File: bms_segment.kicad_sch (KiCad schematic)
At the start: 95 parts, among them J1 CELL_TAPS, J2 I2C, J5 SWD, J6 I2C, SW1 SW_Push, U1 LMR516xx, U2 STM32F103C8Tx, U3 ADuM1252, U4 MAX14920, U5 MAX11163, U6 REF61xx, Y1 8M

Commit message: bom: Cleanup some BOM fields
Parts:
- C34: Dist (none) -> LCSC; Dist # (none) -> C126576; Mfr (none) -> Murata; Mfr # (none) -> GCM1885C2A101JA16D
- J1: value CELL_TAPS -> Conn_01x13
- J2, J6: value I2C -> Conn_01x04
- J5: value SWD -> Conn_01x05
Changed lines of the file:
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@@
 			)
 		)
-		(property "Value" "CELL_TAPS"
+		(property "Value" "Conn_01x13"
 			(at 58.42 113.03 0)
 			(effects
@@
 			)
 		)
-		(property "Value" "I2C"
+		(property "Value" "Conn_01x04"
 			(at 135.89 67.31 0)
 			(effects
@@
 			)
 		)
-		(property "Value" "SWD"
+		(property "Value" "Conn_01x05"
 			(at 270.51 86.3599 0)
 			(effects
@@
 			)
 		)
-		(property "Value" "I2C"
+		(property "Value" "Conn_01x04"
 			(at 153.67 62.23 0)
 			(effects
@@
 			)
 		)
-		(property "Dist #" ""
+		(property "Dist #" "C126576"
 			(at 162.56 156.21 0)
 			(effects
@@
 			)
 		)
-		(property "Mfr" ""
+		(property "Mfr" "Murata"
 			(at 162.56 156.21 0)
 			(effects
@@
 			)
 		)
-		(property "Mfr #" ""
+		(property "Mfr #" "GCM1885C2A101JA16D"
 			(at 162.56 156.21 0)
 			(effects
@@
 			)
 		)
-		(property "Dist" ""
+		(property "Dist" "LCSC"
 			(at 162.56 156.21 0)
 			(effects

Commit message: *: Create a 3V3 plane and switch to new reset button
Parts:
- SW1: footprint Button_Switch_SMD:SW_Push_SPST_NO_Alps_SKRK -> Button_Switch_SMD:SW_Push_1P1T_NO_Vertical_Wuerth_434133025816; Dist # C720477 -> C139797; Mfr XUNPU -> ALPSALPINE; Mfr # TS-1088-AR02016 -> SKRPACE010
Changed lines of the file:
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@@
 			)
 		)
-		(property "Footprint" "Button_Switch_SMD:SW_Push_SPST_NO_Alps_SKRK"
+		(property "Footprint" "Button_Switch_SMD:SW_Push_1P1T_NO_Vertical_Wuerth_434133025816"
 			(at 270.51 95.25 0)
 			(effects
@@
 			)
 		)
-		(property "Dist #" "C720477"
+		(property "Dist #" "C139797"
 			(at 270.51 100.33 0)
 			(effects
@@
 			)
 		)
-		(property "Mfr" "XUNPU"
+		(property "Mfr" "ALPSALPINE"
 			(at 270.51 100.33 0)
 			(effects
@@
 			)
 		)
-		(property "Mfr #" "TS-1088-AR02016"
+		(property "Mfr #" "SKRPACE010"
 			(at 270.51 100.33 0)
 			(effects

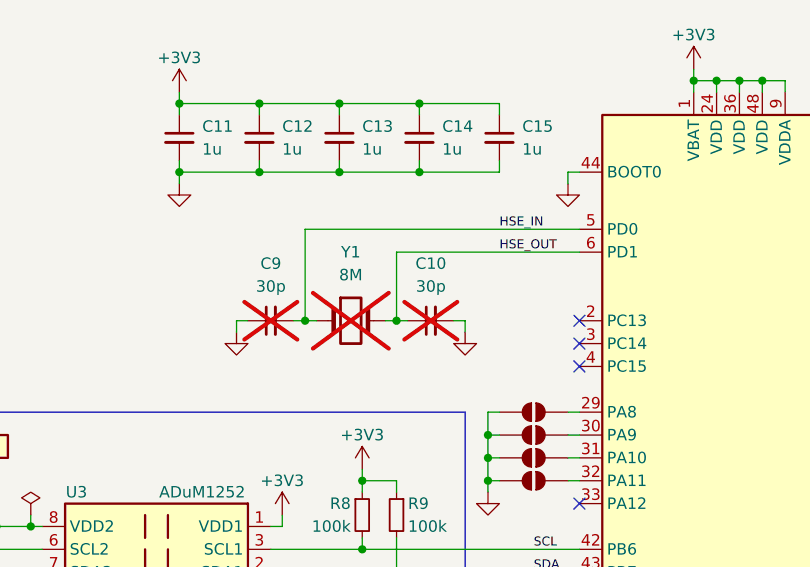
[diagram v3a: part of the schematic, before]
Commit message: schematic: Remove STM crystal
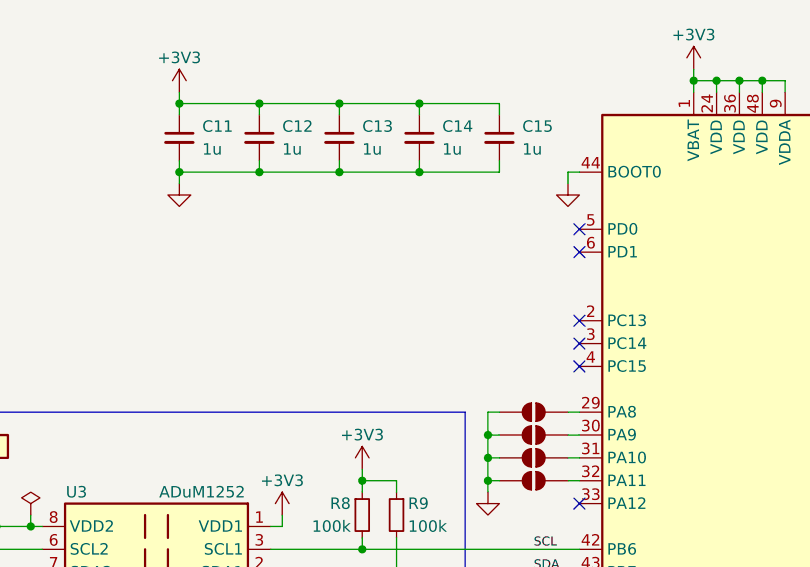
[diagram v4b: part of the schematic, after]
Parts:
- removed C10, C9: 30p, Capacitor_SMD:C_0603_1608Metric, symbol Device:C_Small
- removed Y1: 8M, Crystal:Crystal_SMD_5032-2Pin_5.0x3.2mm, symbol Device:Crystal
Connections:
- net HSE_IN: no longer names the net of U2.5 (PD0)
- net HSE_OUT: no longer names the net of U2.6 (PD1)
- no-connect marks 10 -> 12

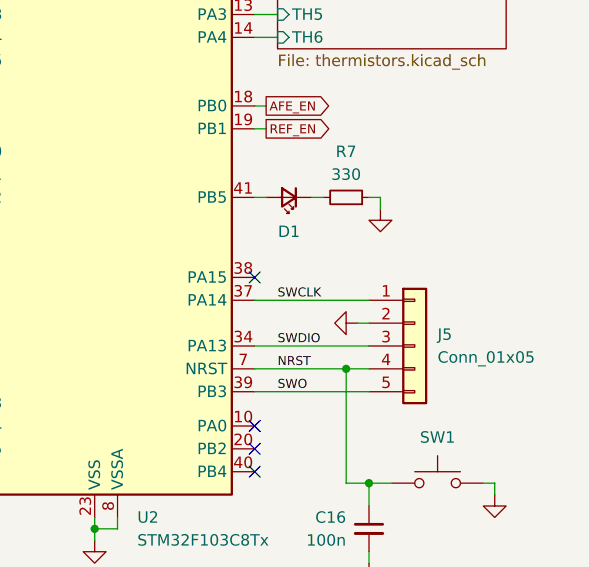
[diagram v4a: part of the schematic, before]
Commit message: schematic: Switch to new SWD header
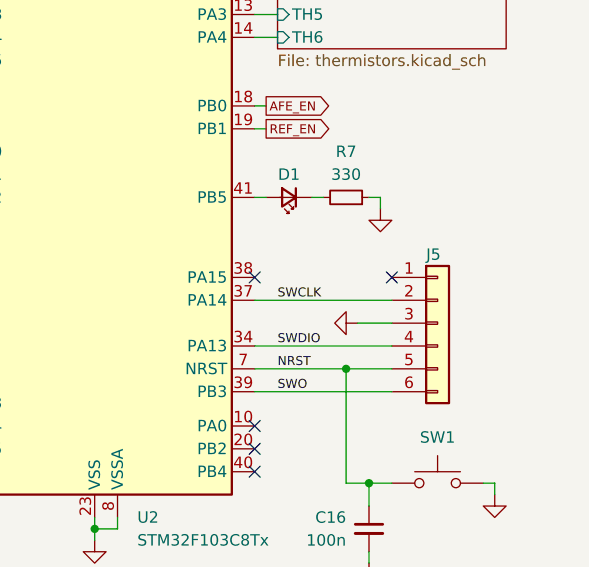
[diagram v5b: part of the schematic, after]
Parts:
- removed J5: Conn_01x05, Connector_PinHeader_2.54mm:PinHeader_1x05_P2.54mm_Vertical, symbol Connector_Generic:Conn_01x05
- added J5: Conn_01x06, yfs:IDC-Connector-2x3, symbol Connector_Generic:Conn_01x06
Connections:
- net GND: now also J5.3 (Pin_3)
- net NRST: now also J5.5 (Pin_5)
- net SWCLK: now also J5.2 (Pin_2)
- net SWDIO: now also J5.4 (Pin_4)
- net SWO: now also J5.6 (Pin_6)
- no-connect marks 12 -> 13
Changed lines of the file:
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@@
 	)
 	(no_connect
+		(at 265.43 77.47)
+	)
+	(no_connect
 		(at 214.63 53.34)
 	)
@@
 	(wire
 		(pts
-			(xy 250.19 85.09) (xy 262.89 85.09)
+			(xy 250.19 85.09) (xy 265.43 85.09)
 		)
 		(stroke
@@
 	(wire
 		(pts
-			(xy 250.19 80.01) (xy 262.89 80.01)
+			(xy 250.19 80.01) (xy 265.43 80.01)
 		)
 		(stroke
@@
 	(wire
 		(pts
-			(xy 250.19 90.17) (xy 262.89 90.17)
+			(xy 250.19 90.17) (xy 265.43 90.17)
 		)
 		(stroke
@@
 	(wire
 		(pts
-			(xy 261.62 82.55) (xy 262.89 82.55)
+			(xy 261.62 82.55) (xy 265.43 82.55)
 		)
 		(stroke
@@
 	(wire
 		(pts
-			(xy 260.35 87.63) (xy 262.89 87.63)
+			(xy 260.35 87.63) (xy 265.43 87.63)
 		)
 		(stroke
@@
 	)
 	(symbol
-		(lib_id "Connector_Generic:Conn_01x05")
-		(at 267.97 85.09 0)
-		(unit 1)
-		(exclude_from_sim no)
-		(in_bom yes)
-		(on_board yes)
-		(dnp no)
-		(fields_autoplaced yes)
-		(property "Reference" "J5"
-			(at 270.51 83.8199 0)
-			(effects
-				(font
-					(size 1.27 1.27)
-				)
-				(justify left)
-			)
-		)
-		(property "Value" "Conn_01x05"
-			(at 270.51 86.3599 0)
-			(effects
-				(font
-					(size 1.27 1.27)
-				)
-				(justify left)
-			)
-		)
-		(property "Footprint" "Connector_PinHeader_2.54mm:PinHeader_1x05_P2.54mm_Vertical"
-			(at 267.97 85.09 0)
-			(effects
-				(font
-					(size 1.27 1.27)
-				)
-				(hide yes)
-			)
-		)
-		(property "Datasheet" "~"
-			(at 267.97 85.09 0)
-			(effects
-				(font
-					(size 1.27 1.27)
-				)
-				(hide yes)
-			)
-		)
-		(property "Description" "Generic connector, single row, 01x05, script generated (kicad-library-utils/schlib/autogen/connector/)"
-			(at 267.97 85.09 0)
-			(effects
-				(font
-					(size 1.27 1.27)
-				)
-				(hide yes)
-			)
-		)
-		(property "Dist #" ""
-			(at 267.97 85.09 0)
-			(effects
-				(font
-					(size 1.27 1.27)
-				)
-				(hide yes)
-			)
-		)
-		(property "Mfr" ""
-			(at 267.97 85.09 0)
-			(effects
-				(font
-					(size 1.27 1.27)
-				)
-				(hide yes)
-			)
-		)
-		(property "Mfr #" ""
-			(at 267.97 85.09 0)
-			(effects
-				(font
-					(size 1.27 1.27)
-				)
-				(hide yes)
-			)
-		)
-		(property "Dist" ""
-			(at 267.97 85.09 0)
-			(effects
-				(font
-					(size 1.27 1.27)
-				)
-				(hide yes)
-			)
-		)
-		(pin "5"
-		)
-		(pin "1"
-		)
-		(pin "4"
-		)
-		(pin "3"
-		)
-		(pin "2"
-		)
-		(instances
-			(project "bms"
-				(path "/ae4a7653-8e6d-4e05-b144-1e5e3b2092b7"
-					(reference "J5")
-					(unit 1)
-				)
-			)
-		)
-	)
-	(symbol
 		(lib_id "power:GND")
 		(at 46.99 46.99 0)
@@
 		(dnp no)
 		(property "Reference" "D1"
-			(at 254 72.39 0)
+			(at 254 66.04 0)
 			(effects
 				(font
@@
 					(unit 1)
 				)
+			)
+		)
+	)
+	(symbol
+		(lib_id "Connector_Generic:Conn_01x06")
+		(at 270.51 82.55 0)
+		(unit 1)
+		(exclude_from_sim no)
+		(in_bom yes)
+		(on_board yes)
+		(dnp no)
+		(property "Reference" "J5"
+			(at 269.24 74.93 0)
+			(effects
+				(font
+					(size 1.27 1.27)
+				)
+				(justify left)
+			)
+		)
+		(property "Value" "Conn_01x06"
+			(at 273.05 85.0899 0)
+			(effects
+				(font
+					(size 1.27 1.27)
+				)
+				(justify left)
+				(hide yes)
+			)
+		)
+		(property "Footprint" "yfs:IDC-Connector-2x3"
+			(at 270.51 82.55 0)
+			(effects
+				(font
+					(size 1.27 1.27)
+				)
+				(hide yes)
+			)
+		)
+		(property "Datasheet" "~"
+			(at 270.51 82.55 0)
+			(effects
+				(font
+					(size 1.27 1.27)
+				)
+				(hide yes)
+			)
+		)
+		(property "Description" "Generic connector, single row, 01x06, script generated (kicad-library-utils/schlib/autogen/connector/)"
+			(at 270.51 82.55 0)
+			(effects
+				(font
+					(size 1.27 1.27)
+				)
+				(hide yes)
+			)
+		)
+		(property "Dist #" "C42372545"
+			(at 270.51 82.55 0)
+			(effects
+				(font
+					(size 1.27 1.27)
+				)
+				(hide yes)
+			)
+		)
+		(property "Mfr" "hanxia"
+			(at 270.51 82.55 0)
+			(effects
+				(font
+					(size 1.27 1.27)
+				)
+				(hide yes)
+			)
+		)
+		(property "Mfr #" "HX JN1.27-2x3P ZZ H4.9"
+			(at 270.51 82.55 0)
+			(effects
+				(font
+					(size 1.27 1.27)
+				)
+				(hide yes)
+			)
+		)
+		(property "Dist" "LCSC"
+			(at 270.51 82.55 0)
+			(effects
+				(font
+					(size 1.27 1.27)
+				)
+				(hide yes)
+			)
+		)
+		(pin "5"
+		)
+		(pin "1"
+		)
+		(pin "4"
+		)
+		(pin "3"
+		)
+		(pin "2"
+		)
+		(pin "6"
+		)
+		(instances
+			(project "bms_segment"
+				(path "/ae4a7653-8e6d-4e05-b144-1e5e3b2092b7"
+					(reference "J5")
+					(unit 1)
+				)

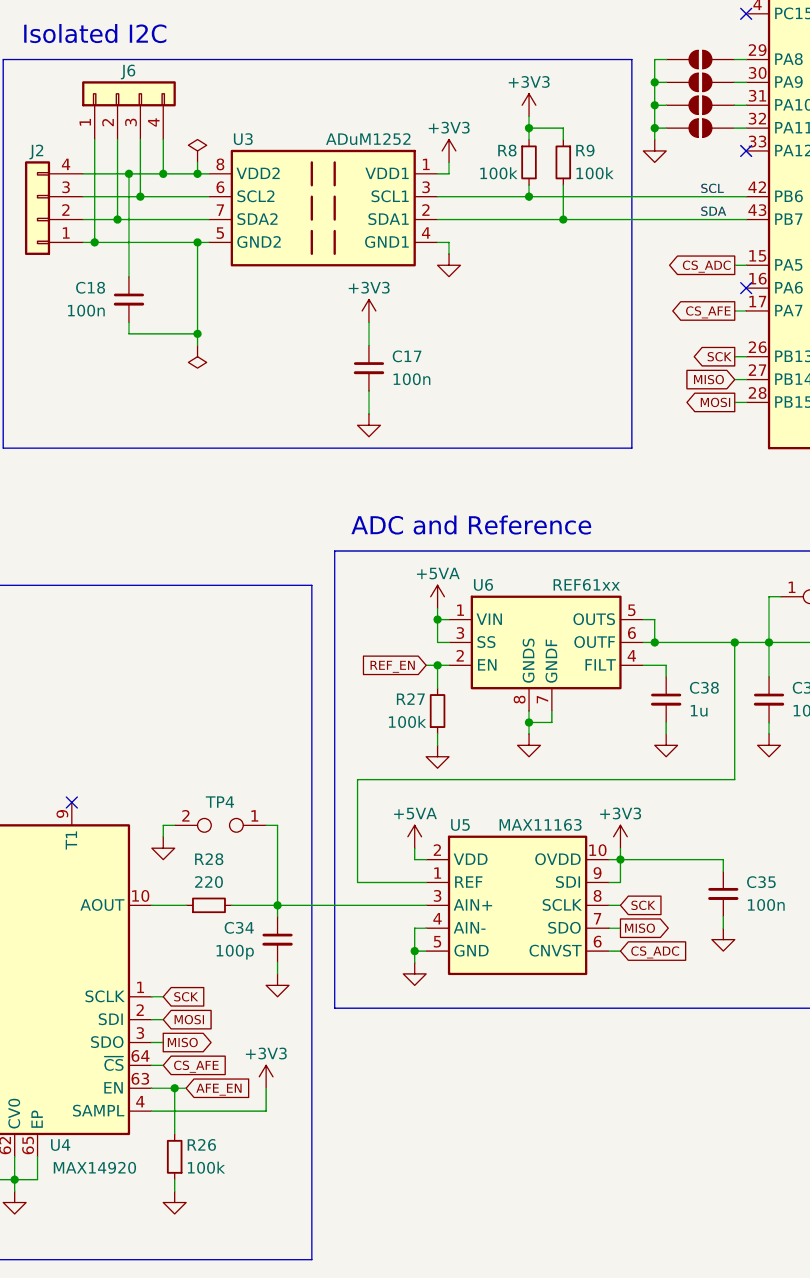
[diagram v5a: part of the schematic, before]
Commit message: schematic: Change all 100k resistors to 10k
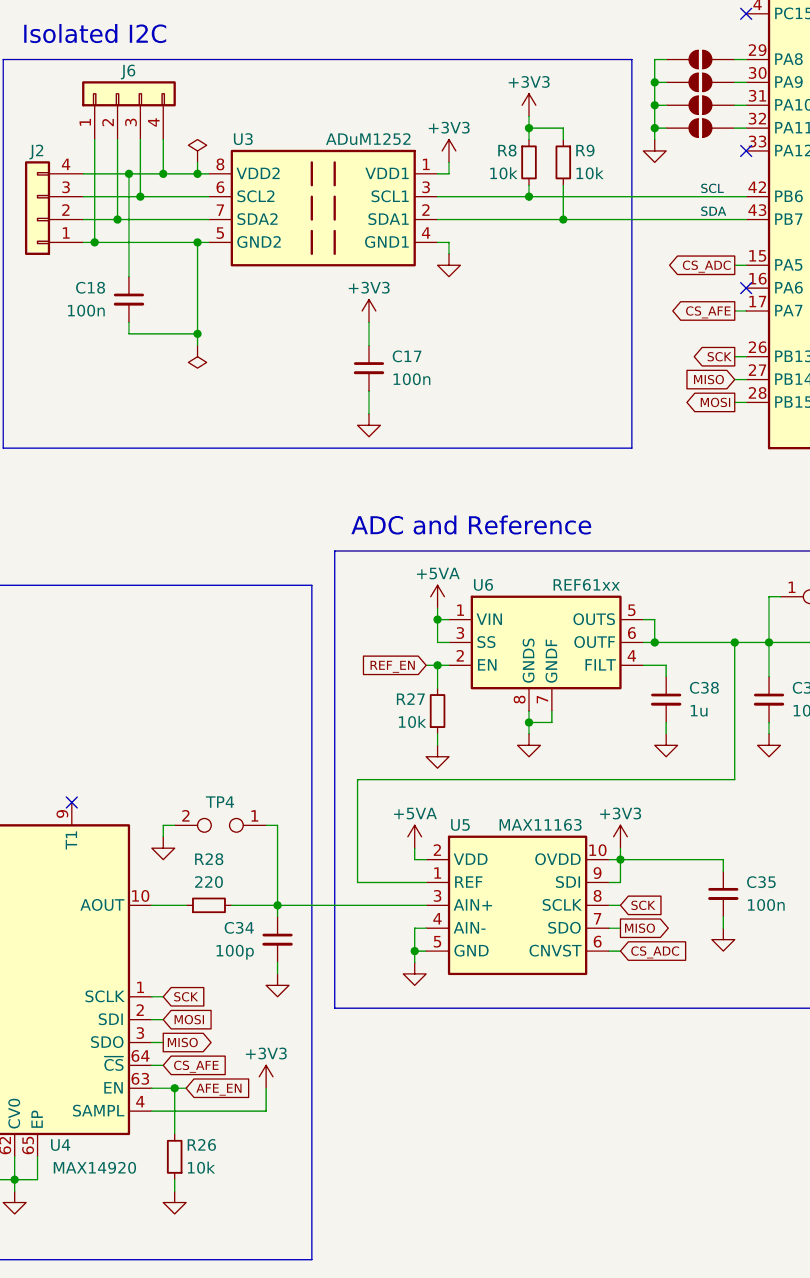
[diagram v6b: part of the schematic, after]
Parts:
- R26, R27, R8, R9: value 100k -> 10k; Dist # C25803 -> C25804; Mfr # 0603WAF1003T5E -> 0603WAF1002T5E
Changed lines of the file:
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@@
 			)
 		)
-		(property "Value" "100k"
+		(property "Value" "10k"
 			(at 189.23 71.12 0)
 			(effects
@@
 			)
 		)
-		(property "Dist #" "C25803"
+		(property "Dist #" "C25804"
 			(at 190.5 69.85 0)
 			(effects
@@
 			)
 		)
-		(property "Mfr #" "0603WAF1003T5E"
+		(property "Mfr #" "0603WAF1002T5E"
 			(at 190.5 69.85 0)
 			(effects
@@
 			)
 		)
-		(property "Value" "100k"
+		(property "Value" "10k"
 			(at 195.58 71.12 0)
 			(effects
@@
 			)
 		)
-		(property "Dist #" "C25803"
+		(property "Dist #" "C25804"
 			(at 194.31 69.85 0)
 			(effects
@@
 			)
 		)
-		(property "Mfr #" "0603WAF1003T5E"
+		(property "Mfr #" "0603WAF1002T5E"
 			(at 194.31 69.85 0)
 			(effects
@@
 			)
 		)
-		(property "Value" "100k"
+		(property "Value" "10k"
 			(at 152.4 181.61 0)
 			(effects
@@
 			)
 		)
-		(property "Dist #" "C25803"
+		(property "Dist #" "C25804"
 			(at 151.13 180.34 0)
 			(effects
@@
 			)
 		)
-		(property "Mfr #" "0603WAF1003T5E"
+		(property "Mfr #" "0603WAF1002T5E"
 			(at 151.13 180.34 0)
 			(effects
@@
 			)
 		)
-		(property "Value" "100k"
+		(property "Value" "10k"
 			(at 179.07 132.08 0)
 			(effects
@@
 			)
 		)
-		(property "Dist #" "C25803"
+		(property "Dist #" "C25804"
 			(at 180.34 130.81 0)
 			(effects
@@
 			)
 		)
-		(property "Mfr #" "0603WAF1003T5E"
+		(property "Mfr #" "0603WAF1002T5E"
 			(at 180.34 130.81 0)
 			(effects

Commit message: schematic: Switch to MAX14921
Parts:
- removed C22, C23, C24, C25, C26, C27, C28, C29, C30, C31, C32, C33: 1u, Capacitor_SMD:C_0805_2012Metric, symbol Device:C_Small
- removed R10, R11, R12, R13, R14, R15, R16, R17, R18, R19, R20, R21: 3k, Resistor_SMD:R_0603_1608Metric, symbol Device:R_Small
- removed R25: 1k, Resistor_SMD:R_0603_1608Metric, symbol Device:R_Small
- removed U4: MAX14920, Package_QFP:TQFP-64-1EP_10x10mm_P0.5mm_EP5.305x5.305mm, symbol yfs:MAX14920
- added C10, C42, C43, C44, C45, C46, C47, C48, C49, C50, C51, C52, C53, C9: 1u, Capacitor_SMD:C_0805_2012Metric, symbol Device:C_Small
- added R65, R66, R67, R68, R69, R70, R71, R72, R73, R74, R75, R76, R77, R78: 3k, Resistor_SMD:R_0603_1608Metric, symbol Device:R_Small
- added U8: MAX14921, Package_QFP:TQFP-80_12x12mm_P0.5mm, symbol yfs:MAX14921
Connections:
- net +3V3: now also U8.4 (SAMPL), U8.5 (VL)
- net +5VA: now also U8.12 (VA)
- net AFE_EN: now also U8.79 (EN)
- net CS_AFE: now also U8.80 (~{CS})
- net GND: now also C53.1, U8.11 (AGND), U8.6 (DGND), U8.78 (CV0)
- net MISO: now also U8.3 (SDO)
- net MOSI: now also U8.2 (SDI)
- net SCK: now also U8.1 (SCLK)
- net TAP1: now also R78.2
- net TAP10: now also R69.2
- net TAP11: now also R68.2
- net TAP12: now also R67.2
- net TAP2: now also R77.2
- net TAP3: now also R76.2
- net TAP4: now also R75.2
- net TAP5: now also R74.2
- net TAP6: now also R73.2
- net TAP7: now also R72.2
- net TAP8: now also R71.2
- net TAP9: now also R70.2
- net at R28.1: now also U8.10 (AOUT)
- net AFE_VIN: no longer names the net of C19.1, FB2.2
- net AFE_VIN: now also U8.13 (LDOIN), U8.14 (VP)
- new net: C42.1, U8.34 (CB12)
- new net: C42.2, U8.33 (CT12)
- new net: R77.1, U8.71 (CV2)
- new net: R70.1, U8.43 (CV9)
- new net: R65.1, U8.15 (CV16), U8.19 (CV15), U8.23 (CV14)
- new net: C9.2, U8.25 (CT14)
- new net: C9.1, U8.26 (CB14)
- new net: R66.1, U8.27 (CV13)
- new net: C10.2, U8.29 (CT13)
- new net: C10.1, U8.30 (CB13)
- new net: R67.1, U8.31 (CV12)
- new net: R68.1, U8.35 (CV11)
- new net: C43.2, U8.37 (CT11)
- new net: C43.1, U8.38 (CB11)
- new net: R69.1, U8.39 (CV10)
- new net: C44.2, U8.41 (CT10)
- new net: C44.1, U8.42 (CB10)
- new net: C45.2, U8.45 (CT9)
- new net: C45.1, U8.46 (CB9)
- new net: R71.1, U8.47 (CV8)
- new net: C46.2, U8.49 (CT8)
- new net: C46.1, U8.50 (CB8)
- new net: R72.1, U8.51 (CV7)
- new net: C47.2, U8.53 (CT7)
- new net: C47.1, U8.54 (CB7)
- new net: R73.1, U8.55 (CV6)
- new net: C48.2, U8.57 (CT6)
- new net: C48.1, U8.58 (CB6)
- new net: R74.1, U8.59 (CV5)
- new net: C49.2, U8.61 (CT5)
- new net: C49.1, U8.62 (CB5)
- new net: R75.1, U8.63 (CV4)
- new net: C50.2, U8.65 (CT4)
- new net: C50.1, U8.66 (CB4)
- new net: R76.1, U8.67 (CV3)
- new net: C51.2, U8.69 (CT3)
- new net: C51.1, U8.70 (CB3)
- new net: C52.2, U8.73 (CT2)
- new net: C52.1, U8.74 (CB2)
- new net: R78.1, U8.75 (CV1)
- new net: C53.2, U8.77 (CT1)
- new net Balancers/BA1: U8.76 (BA1)
- new net Balancers/BA10: U8.40 (BA10)
- new net Balancers/BA11: U8.36 (BA11)
- new net Balancers/BA12: U8.32 (BA12)
- new net Balancers/BA13: U8.28 (BA13)
- new net Balancers/BA14: U8.24 (BA14)
- new net Balancers/BA2: U8.72 (BA2)
- new net Balancers/BA3: U8.68 (BA3)
- new net Balancers/BA4: U8.64 (BA4)
- new net Balancers/BA5: U8.60 (BA5)
- new net Balancers/BA6: U8.56 (BA6)
- new net Balancers/BA7: U8.52 (BA7)
- new net Balancers/BA8: U8.48 (BA8)
- new net Balancers/BA9: U8.44 (BA9)
- new net TAP13: R66.2
- new net TAP14: R65.2
- no-connect marks 13 -> 18
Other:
- sheet Balancers ports: added BA1, BA10, BA11, BA12, BA13, BA14, BA2, BA3, BA4, BA5, BA6, BA7, BA8, BA9; removed none
- moved on the sheet: C1, C11, C12, C13, C14, C15, C16, C17, C18, C19, C2, C20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

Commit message: schematic: Rework thermistor frontend
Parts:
- added C13, C14: 1u, Capacitor_SMD:C_0805_2012Metric, symbol Device:C_Small
- added R25: 10k, Resistor_SMD:R_0603_1608Metric, symbol Device:R_Small
- added R8, R9: 3k, Resistor_SMD:R_0603_1608Metric, symbol Device:R_Small
- renumbered C21 to C10, C19 to C11, C18 to C12, C11 to C15, C17 to C16, C9 to C17, C12 to C18, C10 to C19, C13 to C20, C42 to C21, C43 to C22, C14 to C23, C44 to C24, C15 to C25, C45 to C26, C46 to C27, C47 to C28, C48 to C29, C49 to C30, C50 to C31, C51 to C32, C16 to C33, C52 to C34, C53 to C35, C34 to C36, C38 to C37, C35 to C38, C36 to C40, C40 to C41, C37 to C42, C20 to C9, J2 to J1, J6 to J2, J5 to J3, J1 to J4, R66 to R10, R67 to R11, R68 to R12, R69 to R13, R70 to R14, R71 to R15, R72 to R16, R73 to R17, R74 to R18, R8 to R19, R75 to R20, R76 to R21, R9 to R22, R77 to R23, R78 to R24, R7 to R26, R26 to R27, R27 to R29, R65 to R7, U8 to U2, U2 to U4
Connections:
- net +3V3: now also R25.2
- net SCL: now also U4.10 (PA0)
- net TAP14: now also R9.2; no longer R7.2
- net EXT_REF: now reaches C39.1, C41.1, TP5.1, U5.1 (REF), U6.5 (OUTS), U6.6 (OUTF)
- net at R7.1, U2.15 (CV16): no longer U2.19 (CV15), U2.23 (CV14)
- net Balancers/BA16: now reaches U2.16 (BA16)
- net at U2.17 (CT16): now also C13.2
- net at U2.18 (CB16): now also C13.1
- net Balancers/BA15: now reaches U2.20 (BA15)
- net at U2.21 (CT15): now also C14.2
- net at U2.22 (CB15): now also C14.1
- net at U2.7 (T3): now also R25.1
- net Thermistors/SCL renamed Thermistor Sampling/EN
- net Thermistors/SDA renamed Thermistor Sampling/A
- net Thermistors/TH0 renamed Thermistor Sampling/B
- net Thermistors/TH1 renamed Thermistor Sampling/C
- net Thermistors/TH2: no longer names the net of U4.25 (PB12)
- net Thermistors/TH3 renamed Thermistor Sampling/RAIL
- net Thermistors/TH4 renamed Thermistor Sampling/OUT1
- net Thermistors/TH5 renamed Thermistor Sampling/OUT2
- net Thermistors/TH6 renamed Thermistor Sampling/OUT3
- new net: R8.1, U2.19 (CV15)
- new net: R9.1, U2.23 (CV14)
- new net TAP15: R8.2
- new net TAP16: R7.2
- no-connect marks 18 -> 14
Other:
- removed sheet Thermistors
- added sheet Thermistor Sampling (thermistor_sampling.kicad_sch)
- sheet Balancers ports: added BA15, BA16; removed none
- moved on the sheet: C1, C12, C15, C16, C18, C2, C20, C23, C25, C3, C33, C4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
